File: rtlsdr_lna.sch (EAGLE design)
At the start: 18 parts, among them U1 MIC5205-3

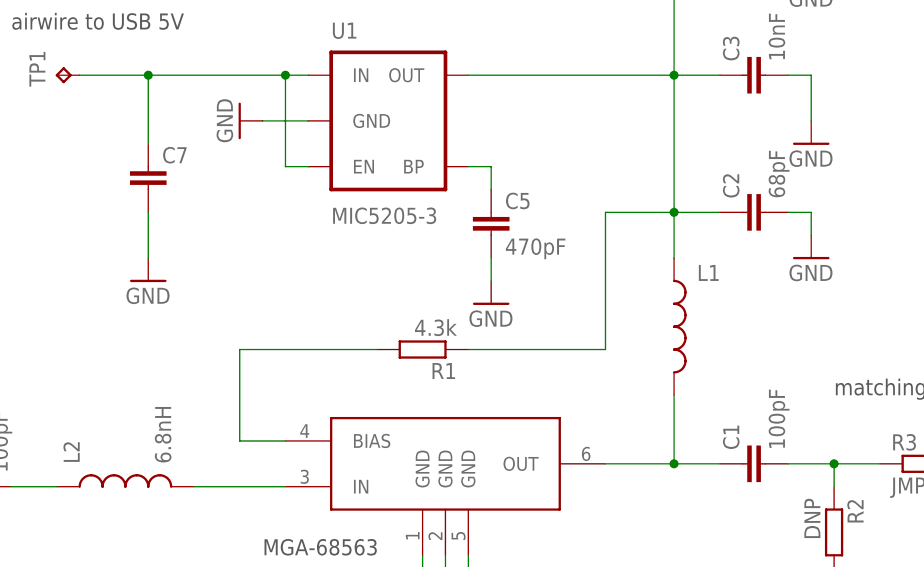
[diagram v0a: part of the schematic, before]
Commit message: increased inductor package size, added missing ldo and rbias component values
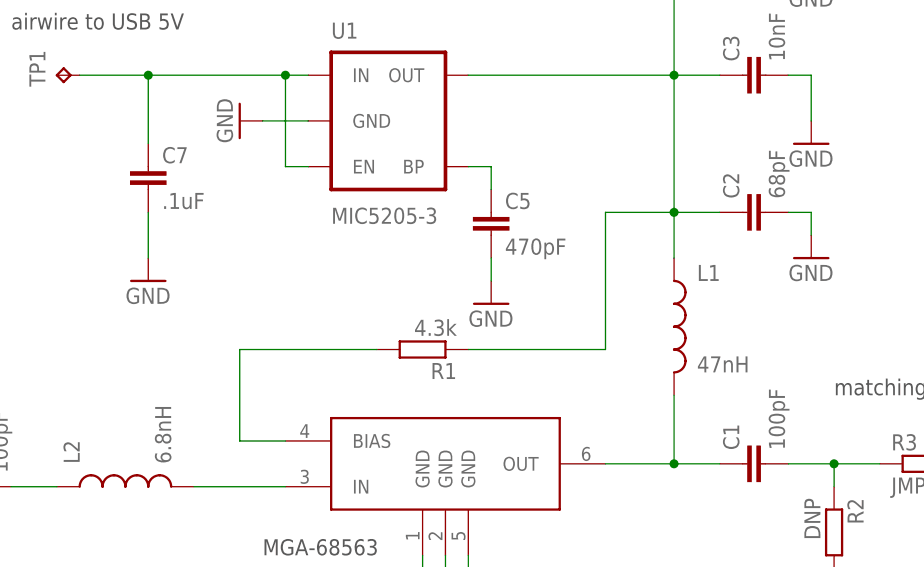
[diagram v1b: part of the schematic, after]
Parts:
- C7: value (none) -> .1uF
- L1: value (none) -> 47nH; device SparkFun-Passives:INDUCTOR0402 -> SparkFun-Passives:INDUCTOR0603
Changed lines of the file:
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@@
 <grid distance="0.1" unitdist="inch" unit="inch" style="lines" multiple="1" display="no" altdistance="0.01" altunitdist="inch" altunit="inch"/>
 <layers>
-<layer number="1" name="Top" color="4" fill="1" visible="no" active="no"/>
-<layer number="16" name="Bottom" color="1" fill="1" visible="no" active="no"/>
-<layer number="17" name="Pads" color="2" fill="1" visible="no" active="no"/>
-<layer number="18" name="Vias" color="2" fill="1" visible="no" active="no"/>
-<layer number="19" name="Unrouted" color="6" fill="1" visible="no" active="no"/>
-<layer number="20" name="Dimension" color="15" fill="1" visible="no" active="no"/>
-<layer number="21" name="tPlace" color="7" fill="1" visible="no" active="no"/>
-<layer number="22" name="bPlace" color="7" fill="1" visible="no" active="no"/>
-<layer number="23" name="tOrigins" color="15" fill="1" visible="no" active="no"/>
-<layer number="24" name="bOrigins" color="15" fill="1" visible="no" active="no"/>
-<layer number="25" name="tNames" color="7" fill="1" visible="no" active="no"/>
-<layer number="26" name="bNames" color="7" fill="1" visible="no" active="no"/>
-<layer number="27" name="tValues" color="7" fill="1" visible="no" active="no"/>
-<layer number="28" name="bValues" color="7" fill="1" visible="no" active="no"/>
+<layer number="1" name="Top" color="4" fill="1" visible="yes" active="no"/>
+<layer number="16" name="Bottom" color="1" fill="1" visible="yes" active="no"/>
+<layer number="17" name="Pads" color="2" fill="1" visible="yes" active="no"/>
+<layer number="18" name="Vias" color="2" fill="1" visible="yes" active="no"/>
+<layer number="19" name="Unrouted" color="6" fill="1" visible="yes" active="no"/>
+<layer number="20" name="Dimension" color="15" fill="1" visible="yes" active="no"/>
+<layer number="21" name="tPlace" color="7" fill="1" visible="yes" active="no"/>
+<layer number="22" name="bPlace" color="7" fill="1" visible="yes" active="no"/>
+<layer number="23" name="tOrigins" color="15" fill="1" visible="yes" active="no"/>
+<layer number="24" name="bOrigins" color="15" fill="1" visible="yes" active="no"/>
+<layer number="25" name="tNames" color="7" fill="1" visible="yes" active="no"/>
+<layer number="26" name="bNames" color="7" fill="1" visible="yes" active="no"/>
+<layer number="27" name="tValues" color="7" fill="1" visible="yes" active="no"/>
+<layer number="28" name="bValues" color="7" fill="1" visible="yes" active="no"/>
 <layer number="29" name="tStop" color="7" fill="3" visible="no" active="no"/>
 <layer number="30" name="bStop" color="7" fill="6" visible="no" active="no"/>
@@
 <layer number="35" name="tGlue" color="7" fill="4" visible="no" active="no"/>
 <layer number="36" name="bGlue" color="7" fill="5" visible="no" active="no"/>
-<layer number="37" name="tTest" color="7" fill="1" visible="no" active="no"/>
-<layer number="38" name="bTest" color="7" fill="1" visible="no" active="no"/>
+<layer number="37" name="tTest" color="7" fill="1" visible="yes" active="no"/>
+<layer number="38" name="bTest" color="7" fill="1" visible="yes" active="no"/>
 <layer number="39" name="tKeepout" color="4" fill="11" visible="no" active="no"/>
 <layer number="40" name="bKeepout" color="1" fill="11" visible="no" active="no"/>
@@
 <layer number="44" name="Drills" color="7" fill="1" visible="no" active="no"/>
 <layer number="45" name="Holes" color="7" fill="1" visible="no" active="no"/>
-<layer number="46" name="Milling" color="3" fill="1" visible="no" active="no"/>
-<layer number="47" name="Measures" color="7" fill="1" visible="no" active="no"/>
-<layer number="48" name="Document" color="7" fill="1" visible="no" active="no"/>
-<layer number="49" name="Reference" color="7" fill="1" visible="no" active="no"/>
-<layer number="50" name="dxf" color="7" fill="1" visible="no" active="no"/>
-<layer number="51" name="tDocu" color="7" fill="1" visible="no" active="no"/>
-<layer number="52" name="bDocu" color="7" fill="1" visible="no" active="no"/>
-<layer number="53" name="tGND_GNDA" color="7" fill="9" visible="no" active="no"/>
-<layer number="54" name="bGND_GNDA" color="1" fill="9" visible="no" active="no"/>
-<layer number="56" name="wert" color="7" fill="1" visible="no" active="no"/>
+<layer number="46" name="Milling" color="3" fill="1" visible="yes" active="no"/>
+<layer number="47" name="Measures" color="7" fill="1" visible="yes" active="no"/>
+<layer number="48" name="Document" color="7" fill="1" visible="yes" active="no"/>
+<layer number="49" name="Reference" color="7" fill="1" visible="yes" active="no"/>
+<layer number="50" name="dxf" color="7" fill="1" visible="yes" active="no"/>
+<layer number="51" name="tDocu" color="7" fill="1" visible="yes" active="no"/>
+<layer number="52" name="bDocu" color="7" fill="1" visible="yes" active="no"/>
+<layer number="53" name="tGND_GNDA" color="7" fill="9" visible="yes" active="no"/>
+<layer number="54" name="bGND_GNDA" color="1" fill="9" visible="yes" active="no"/>
+<layer number="56" name="wert" color="7" fill="1" visible="yes" active="no"/>
 <layer number="91" name="Nets" color="2" fill="1" visible="yes" active="yes"/>
 <layer number="92" name="Busses" color="1" fill="1" visible="yes" active="yes"/>
@@
 <part name="C4" library="rcl" deviceset="C-EU" device="C0402" value="100pF"/>
 <part name="FRAME1" library="frames" deviceset="LETTER_L" device=""/>
-<part name="L1" library="SparkFun-Passives" deviceset="INDUCTOR" device="0402"/>
+<part name="L1" library="SparkFun-Passives" deviceset="INDUCTOR" device="0603" value="47nH"/>
 <part name="R2" library="rcl" deviceset="R-EU_" device="R0402" value="DNP"/>
 <part name="R3" library="rcl" deviceset="R-EU_" device="R0402" value="JMP"/>
@@
 <part name="TP1" library="testpad" deviceset="TP" device="TP20SQ"/>
 <part name="C6" library="rcl" deviceset="C-EU" device="C0805" value="4.7uF, TANT"/>
-<part name="C7" library="rcl" deviceset="C-EU" device="C0603"/>
+<part name="C7" library="rcl" deviceset="C-EU" device="C0603" value=".1uF"/>
 <part name="GND11" library="supply1" deviceset="GND" device=""/>
 </parts>

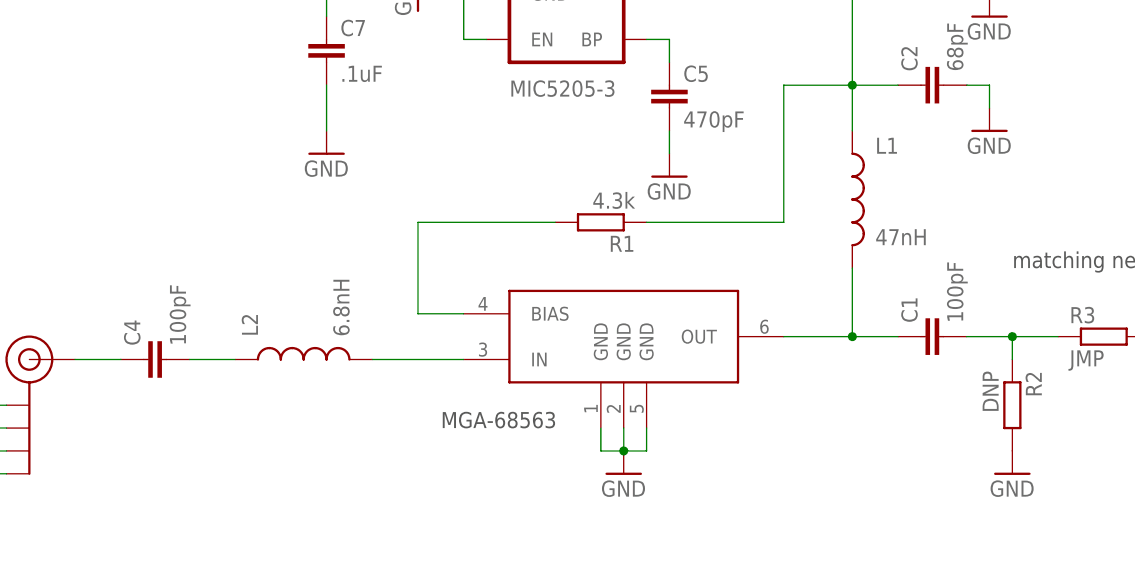
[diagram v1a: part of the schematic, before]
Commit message: changed values in matching network for improved S11 at lower frequencies (increased DC bias inductor value, increased DC blocking capacitor values to 330pF)
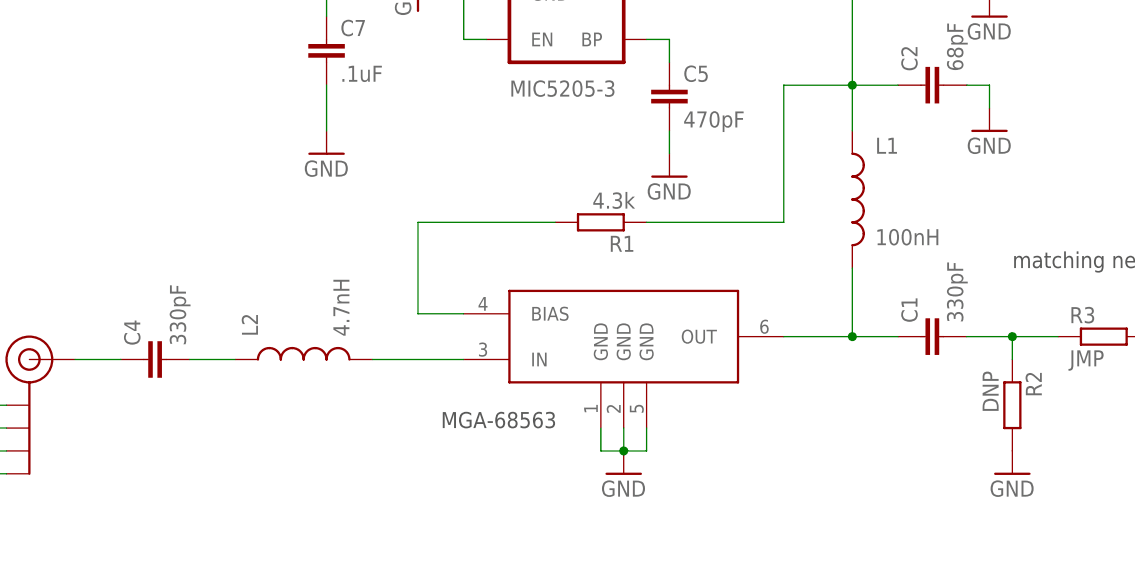
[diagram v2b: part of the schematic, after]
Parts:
- C1, C4: value 100pF -> 330pF
- L1: value 47nH -> 100nH
- L2: value 6.8nH -> 4.7nH
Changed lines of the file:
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@@
 <grid distance="0.1" unitdist="inch" unit="inch" style="lines" multiple="1" display="no" altdistance="0.01" altunitdist="inch" altunit="inch"/>
 <layers>
-<layer number="1" name="Top" color="4" fill="1" visible="yes" active="no"/>
-<layer number="16" name="Bottom" color="1" fill="1" visible="yes" active="no"/>
-<layer number="17" name="Pads" color="2" fill="1" visible="yes" active="no"/>
-<layer number="18" name="Vias" color="2" fill="1" visible="yes" active="no"/>
-<layer number="19" name="Unrouted" color="6" fill="1" visible="yes" active="no"/>
-<layer number="20" name="Dimension" color="15" fill="1" visible="yes" active="no"/>
-<layer number="21" name="tPlace" color="7" fill="1" visible="yes" active="no"/>
-<layer number="22" name="bPlace" color="7" fill="1" visible="yes" active="no"/>
-<layer number="23" name="tOrigins" color="15" fill="1" visible="yes" active="no"/>
-<layer number="24" name="bOrigins" color="15" fill="1" visible="yes" active="no"/>
-<layer number="25" name="tNames" color="7" fill="1" visible="yes" active="no"/>
-<layer number="26" name="bNames" color="7" fill="1" visible="yes" active="no"/>
-<layer number="27" name="tValues" color="7" fill="1" visible="yes" active="no"/>
-<layer number="28" name="bValues" color="7" fill="1" visible="yes" active="no"/>
+<layer number="1" name="Top" color="4" fill="1" visible="no" active="no"/>
+<layer number="16" name="Bottom" color="1" fill="1" visible="no" active="no"/>
+<layer number="17" name="Pads" color="2" fill="1" visible="no" active="no"/>
+<layer number="18" name="Vias" color="2" fill="1" visible="no" active="no"/>
+<layer number="19" name="Unrouted" color="6" fill="1" visible="no" active="no"/>
+<layer number="20" name="Dimension" color="15" fill="1" visible="no" active="no"/>
+<layer number="21" name="tPlace" color="7" fill="1" visible="no" active="no"/>
+<layer number="22" name="bPlace" color="7" fill="1" visible="no" active="no"/>
+<layer number="23" name="tOrigins" color="15" fill="1" visible="no" active="no"/>
+<layer number="24" name="bOrigins" color="15" fill="1" visible="no" active="no"/>
+<layer number="25" name="tNames" color="7" fill="1" visible="no" active="no"/>
+<layer number="26" name="bNames" color="7" fill="1" visible="no" active="no"/>
+<layer number="27" name="tValues" color="7" fill="1" visible="no" active="no"/>
+<layer number="28" name="bValues" color="7" fill="1" visible="no" active="no"/>
 <layer number="29" name="tStop" color="7" fill="3" visible="no" active="no"/>
 <layer number="30" name="bStop" color="7" fill="6" visible="no" active="no"/>
@@
 <layer number="35" name="tGlue" color="7" fill="4" visible="no" active="no"/>
 <layer number="36" name="bGlue" color="7" fill="5" visible="no" active="no"/>
-<layer number="37" name="tTest" color="7" fill="1" visible="yes" active="no"/>
-<layer number="38" name="bTest" color="7" fill="1" visible="yes" active="no"/>
+<layer number="37" name="tTest" color="7" fill="1" visible="no" active="no"/>
+<layer number="38" name="bTest" color="7" fill="1" visible="no" active="no"/>
 <layer number="39" name="tKeepout" color="4" fill="11" visible="no" active="no"/>
 <layer number="40" name="bKeepout" color="1" fill="11" visible="no" active="no"/>
@@
 <layer number="44" name="Drills" color="7" fill="1" visible="no" active="no"/>
 <layer number="45" name="Holes" color="7" fill="1" visible="no" active="no"/>
-<layer number="46" name="Milling" color="3" fill="1" visible="yes" active="no"/>
-<layer number="47" name="Measures" color="7" fill="1" visible="yes" active="no"/>
-<layer number="48" name="Document" color="7" fill="1" visible="yes" active="no"/>
-<layer number="49" name="Reference" color="7" fill="1" visible="yes" active="no"/>
-<layer number="50" name="dxf" color="7" fill="1" visible="yes" active="no"/>
-<layer number="51" name="tDocu" color="7" fill="1" visible="yes" active="no"/>
-<layer number="52" name="bDocu" color="7" fill="1" visible="yes" active="no"/>
-<layer number="53" name="tGND_GNDA" color="7" fill="9" visible="yes" active="no"/>
-<layer number="54" name="bGND_GNDA" color="1" fill="9" visible="yes" active="no"/>
-<layer number="56" name="wert" color="7" fill="1" visible="yes" active="no"/>
+<layer number="46" name="Milling" color="3" fill="1" visible="no" active="no"/>
+<layer number="47" name="Measures" color="7" fill="1" visible="no" active="no"/>
+<layer number="48" name="Document" color="7" fill="1" visible="no" active="no"/>
+<layer number="49" name="Reference" color="7" fill="1" visible="no" active="no"/>
+<layer number="50" name="dxf" color="7" fill="1" visible="no" active="no"/>
+<layer number="51" name="tDocu" color="7" fill="1" visible="no" active="no"/>
+<layer number="52" name="bDocu" color="7" fill="1" visible="no" active="no"/>
+<layer number="53" name="tGND_GNDA" color="7" fill="9" visible="no" active="no"/>
+<layer number="54" name="bGND_GNDA" color="1" fill="9" visible="no" active="no"/>
+<layer number="56" name="wert" color="7" fill="1" visible="no" active="no"/>
 <layer number="91" name="Nets" color="2" fill="1" visible="yes" active="yes"/>
 <layer number="92" name="Busses" color="1" fill="1" visible="yes" active="yes"/>
@@
 <part name="GND1" library="supply1" deviceset="GND" device=""/>
 <part name="R1" library="rcl" deviceset="R-EU_" device="R0402" value="4.3k"/>
-<part name="C1" library="rcl" deviceset="C-EU" device="C0402" value="100pF"/>
+<part name="C1" library="rcl" deviceset="C-EU" device="C0402" value="330pF"/>
 <part name="C2" library="rcl" deviceset="C-EU" device="C0402" value="68pF"/>
 <part name="C3" library="rcl" deviceset="C-EU" device="C0402" value="10nF"/>
-<part name="C4" library="rcl" deviceset="C-EU" device="C0402" value="100pF"/>
+<part name="C4" library="rcl" deviceset="C-EU" device="C0402" value="330pF"/>
 <part name="FRAME1" library="frames" deviceset="LETTER_L" device=""/>
-<part name="L1" library="SparkFun-Passives" deviceset="INDUCTOR" device="0603" value="47nH"/>
+<part name="L1" library="SparkFun-Passives" deviceset="INDUCTOR" device="0603" value="100nH"/>
 <part name="R2" library="rcl" deviceset="R-EU_" device="R0402" value="DNP"/>
 <part name="R3" library="rcl" deviceset="R-EU_" device="R0402" value="JMP"/>
@@
 <part name="GND7" library="supply1" deviceset="GND" device=""/>
 <part name="GND8" library="supply1" deviceset="GND" device=""/>
-<part name="L2" library="SparkFun-Passives" deviceset="INDUCTOR" device="0402" value="6.8nH"/>
+<part name="L2" library="SparkFun-Passives" deviceset="INDUCTOR" device="0402" value="4.7nH"/>
 <part name="J$1" library="SparkFun-Connectors" deviceset="SMA_EDGE" device=""/>
 <part name="GND9" library="supply1" deviceset="GND" device=""/>
